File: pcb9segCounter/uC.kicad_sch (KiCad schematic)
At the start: 14 parts, among them J1 AVR-ISP-6, J2 SAO, U1 ATtiny84A-SS

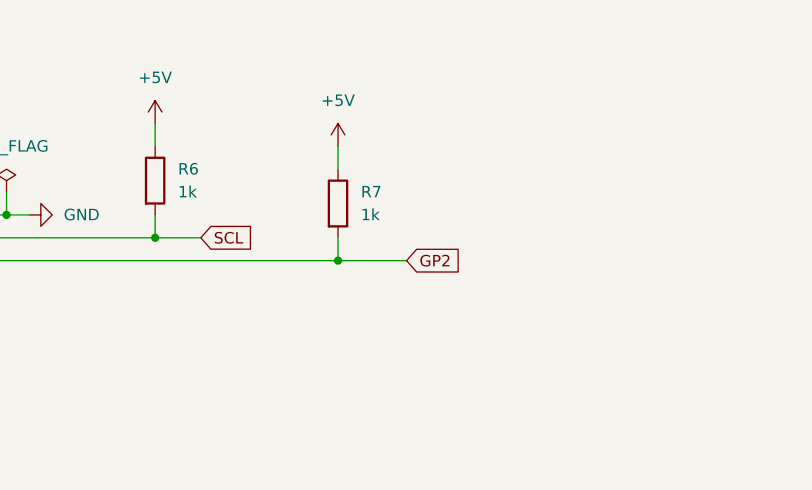
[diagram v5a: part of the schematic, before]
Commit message: Edits to Readme, found error in the schematic and made a note of it, added EEPROM capability to the code.
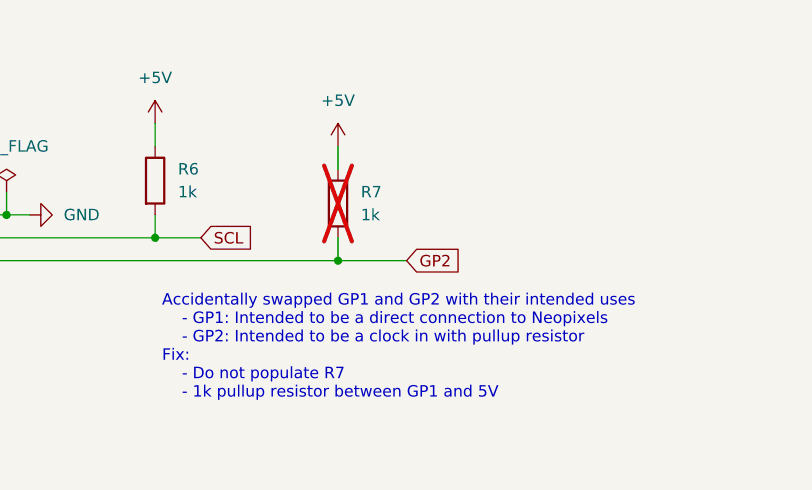
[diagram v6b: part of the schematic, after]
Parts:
- R7: now not fitted
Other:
- note added: "Accidentally swapped GP1 and GP2 with their intended uses - GP1: Intended to be a direct connection to Neopixels - GP2: Intended to be a clock in with pullup resistor Fix: - Do not populate R7 - 1k pullup resistor between GP1 and 5V"
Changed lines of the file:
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@@
+		)
+	)
+	(text "Accidentally swapped GP1 and GP2 with their intended uses\n	- GP1: Intended to be a direct connection to Neopixels\n	- GP2: Intended to be a clock in with pullup resistor\nFix:\n	- Do not populate R7\n	- 1k pullup resistor between GP1 and 5V"
+		(exclude_from_sim no)
+		(at 223.012 154.432 0)
+		(effects
+			(font
+				(size 1.27 1.27)
+			)
+			(justify left)
 		)
 	)
@@
 		(in_bom yes)
 		(on_board yes)
-		(dnp no)
+		(dnp yes)
 		(fields_autoplaced yes)
 		(property "Reference" "R7"

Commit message: Doing lots of cleanup
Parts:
- R5, R6: value 1k -> 4.7k; now not fitted
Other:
- note added: "Accidentally swapped GP1 and GP2 with their intended uses - GP1: Intended to be a direct connection to Neopixels - GP2: Intended to be a clock in with pullup resistor Fix: - Do not populate R7"
- note added: "Buttons"
- note added: "Do not populate R5 and R6, I2C pullups should be on the controller"
- note added: "SAO"
- note removed: "Accidentally swapped GP1 and GP2 with their intended uses - GP1: Intended to be a direct connection to Neopixels - GP2: Intended to be a clock in with pullup resistor Fix: - Do not populate R7 - 1k pullup resistor between GP1 and 5V"
- company: (none) -> Ryan Martin
- title: (none) -> Nine Segment SAO
- moved on the sheet: C19, J1, J2, R2, R3, R4, R7, SW1, SW2, SW3, SW4, U1
